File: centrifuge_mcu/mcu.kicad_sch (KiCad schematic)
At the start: 21 parts, among them J1 Conn_02x10_Odd_Even

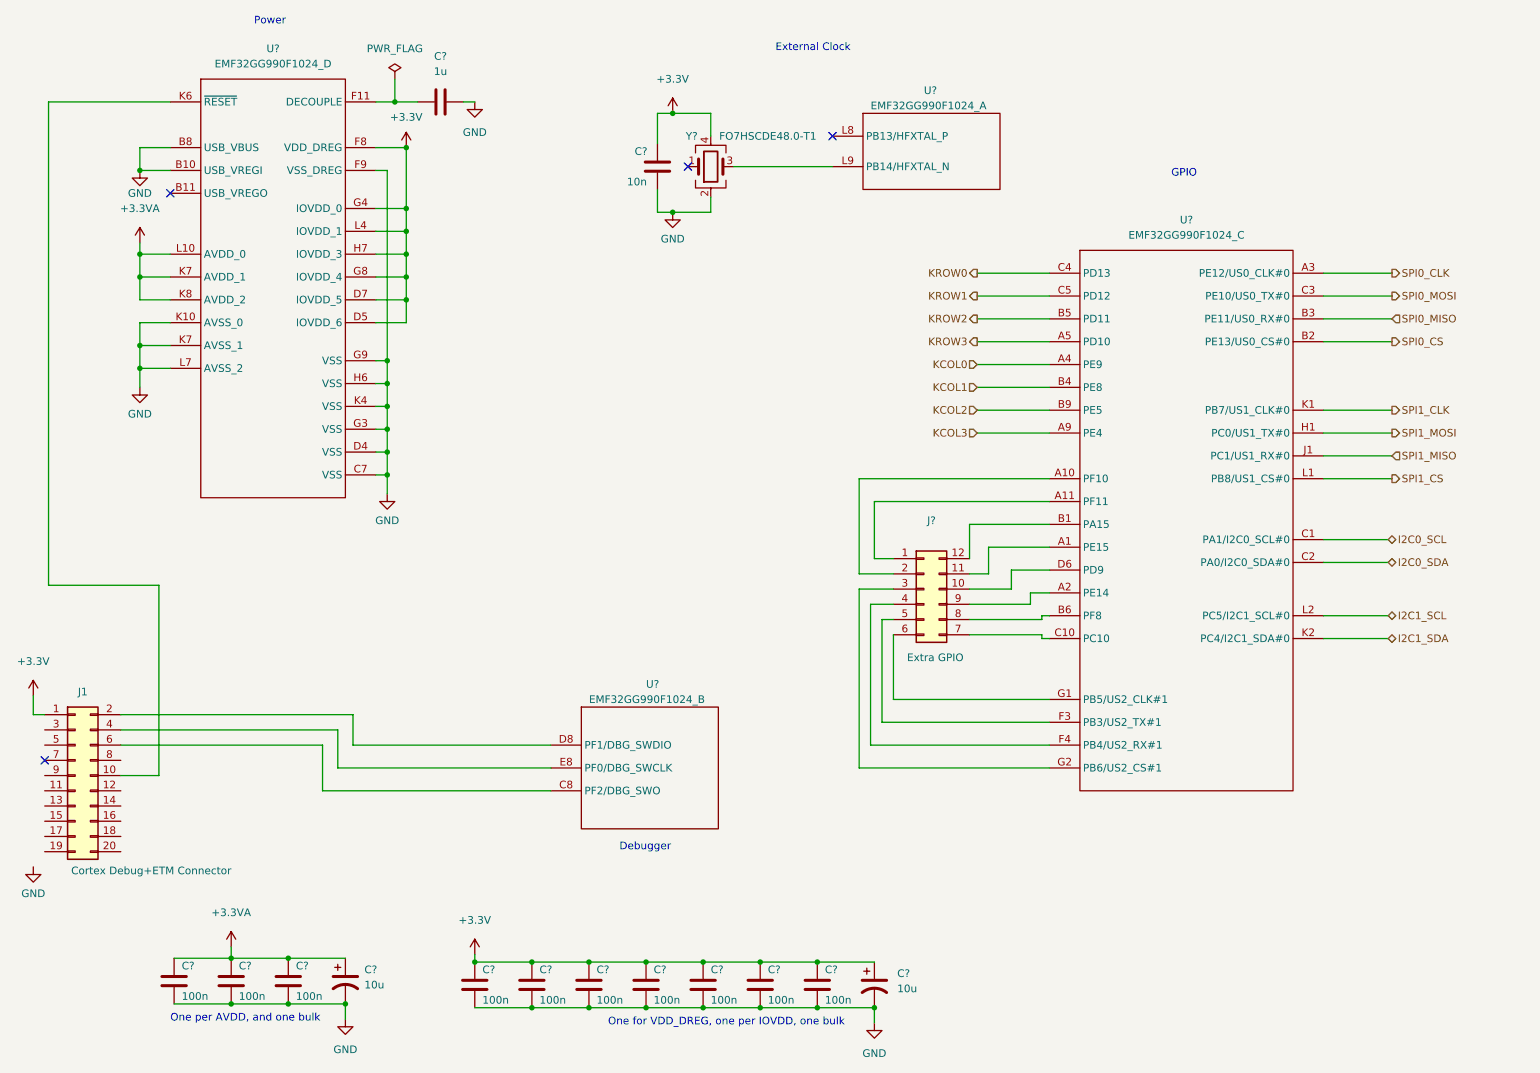
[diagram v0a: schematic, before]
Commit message: make and pick footprints for almost everything
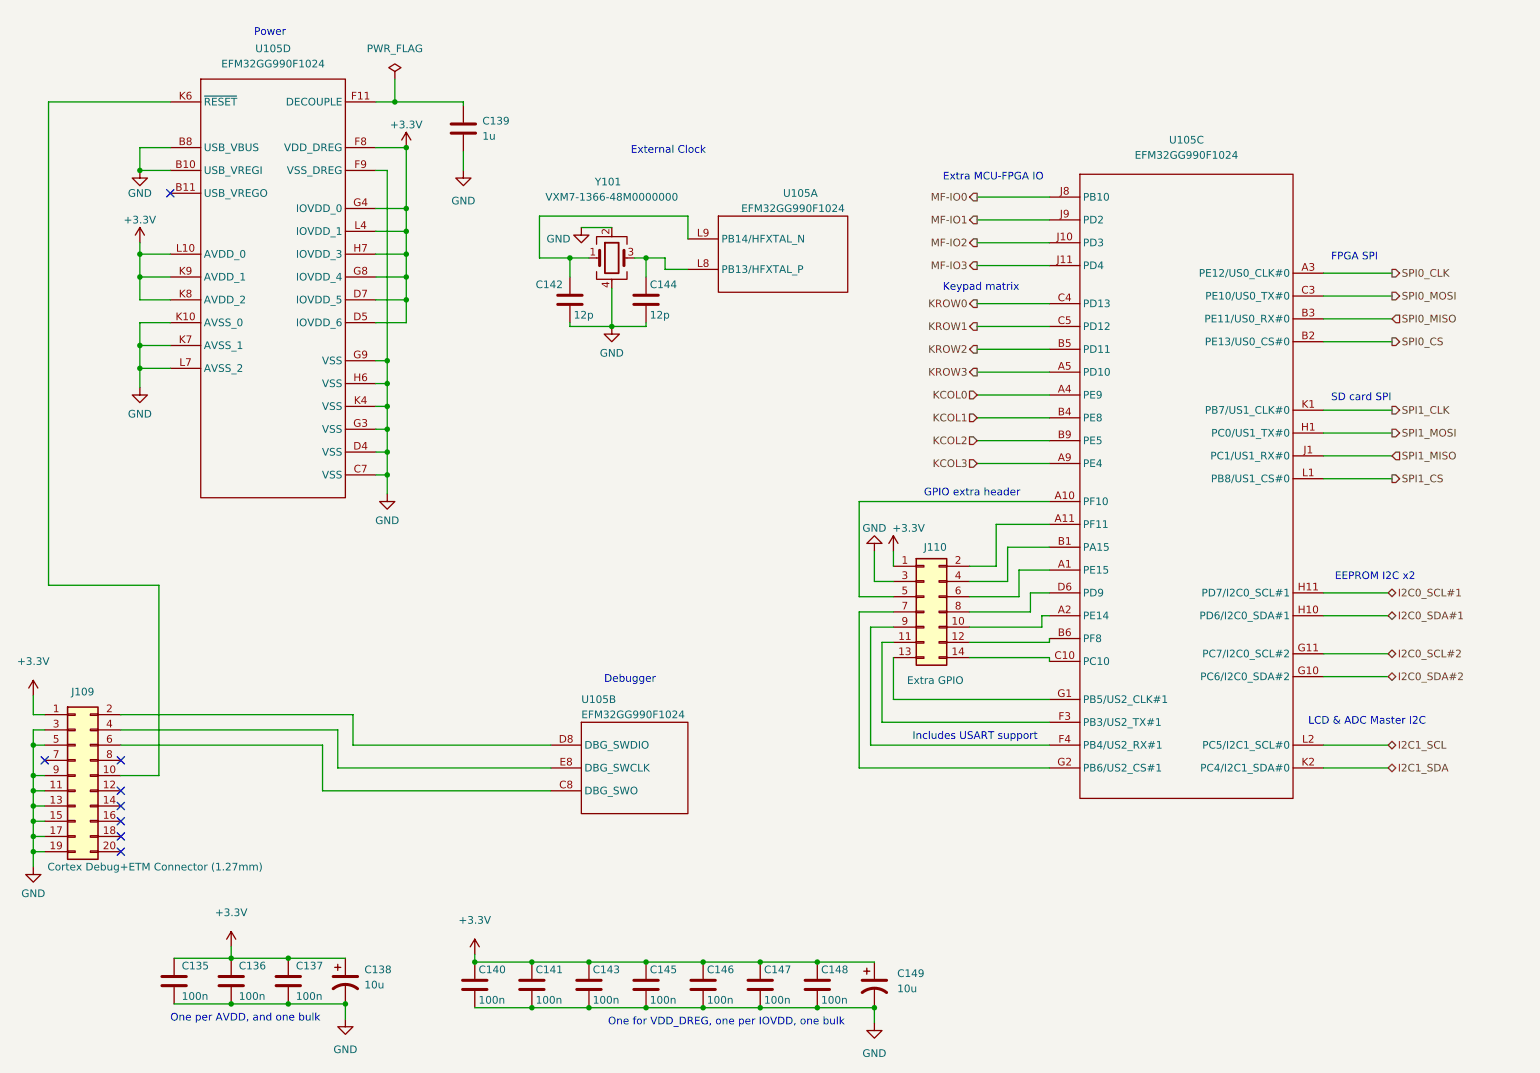
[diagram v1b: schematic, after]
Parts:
- removed C?: 10n, symbol Device:C
- removed U?: EMF32GG990F1024_B, symbol mcu_centrifuge_library:EMF32GG990F1024_B
- removed U?: EMF32GG990F1024_C, symbol mcu_centrifuge_library:EMF32GG990F1024_C
- removed U?: EMF32GG990F1024_D, symbol mcu_centrifuge_library:EMF32GG990F1024_D
- removed U?: EMF32GG990F1024_A, symbol mcu_centrifuge_library:EMF32GG990F1024_A
- removed Y?: FO7HSCDE48.0-T1, symbol Device:Crystal_GND24
- added C142, C144: 12p, Capacitor_SMD:C_0805_2012Metric_Pad1.18x1.45mm_HandSolder, symbol Device:C
- added U105: EFM32GG990F1024, symbol mcu_centrifuge_library:EFM32GG990F1024
- added Y101: VXM7-1366-48M0000000, Crystal:Crystal_SMD_TXC_7M-4Pin_3.2x2.5mm_HandSoldering, symbol Device:Crystal_GND24
- C135, C136, C137, C140, C141, C143, C145, C146, C147, C148: renamed from C?; footprint (none) -> Capacitor_SMD:C_0805_2012Metric_Pad1.18x1.45mm_HandSolder; Purchase (none) -> https://www.digikey.no/no/products/detail/taiyo-yuden/LMF21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
- C138, C149: renamed from C?; footprint (none) -> Capacitor_SMD:CP_Elec_4x5.4; Purchase (none) -> https://www.digikey.no/no/products/detail/nichicon/UWT1C100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
- C139: renamed from C?; footprint (none) -> Capacitor_SMD:C_0805_2012Metric_Pad1.18x1.45mm_HandSolder; Purchase (none) -> https://www.digikey.no/no/products/detail/kemet/C0805C105J4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
- J109: renamed from J1; footprint (none) -> Connector_PinHeader_1.27mm:PinHeader_2x10_P1.27mm_Vertical; Size Cortex Debug+ETM Connector -> Cortex Debug+ETM Connector (1.27mm)
- J110: renamed from J?; value Conn_02x06_Counter_Clockwise -> Conn_02x07_Counter_Clockwise; footprint (none) -> Connector_PinHeader_2.54mm:PinHeader_2x07_P2.54mm_Vertical; symbol Connector_Generic:Conn_02x06_Counter_Clockwise -> Connector_Generic:Conn_02x07_Odd_Even
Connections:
- net +3.3VA is gone; now on net +3.3V: C135.1, C136.1, C137.1, C138.1
- net +3.3V: now also J110.1 (Pin_1), U105.D5 (IOVDD_6), U105.D7 (IOVDD_5), U105.F8 (VDD_DREG), U105.G4 (IOVDD_0), U105.G8 (IOVDD_4), U105.H7 (IOVDD_3), U105.K8 (AVDD_2), U105.K9 (AVDD_1), U105.L10 (AVDD_0), U105.L4 (IOVDD_1)
- net GND: now also C139.1, J109.11 (Pin_11), J109.13 (Pin_13), J109.15 (Pin_15), J109.17 (Pin_17), J109.19 (Pin_19), J109.3 (Pin_3), J109.5 (Pin_5), J109.9 (Pin_9), J110.3 (Pin_3), C142.2, C144.2, U105.B10 (USB_VREGI), U105.B8 (USB_VBUS), U105.C7 (VSS), U105.D4 (VSS), U105.F9 (VSS_DREG), U105.G3 (VSS), U105.G9 (VSS), U105.H6 (VSS), U105.K10 (AVSS_0), U105.K4 (VSS), U105.K7 (AVSS_1), U105.L7 (AVSS_2), Y101.2, Y101.4; no longer C139.2
- net I2C1_SCL: now also U105.L2 (PC5/I2C1_SCL#0)
- net I2C1_SDA: now also U105.K2 (PC4/I2C1_SDA#0)
- net KCOL0: now also U105.A4 (PE9)
- net KCOL1: now also U105.B4 (PE8)
- net KCOL2: now also U105.B9 (PE5)
- net KCOL3: now also U105.A9 (PE4)
- net KROW0: now also U105.C4 (PD13)
- net KROW1: now also U105.C5 (PD12)
- net KROW2: now also U105.B5 (PD11)
- net KROW3: now also U105.A5 (PD10)
- net SPI0_CLK: now also U105.A3 (PE12/US0_CLK#0)
- net SPI0_CS: now also U105.B2 (PE13/US0_CS#0)
- net SPI0_MISO: now also U105.B3 (PE11/US0_RX#0)
- net SPI0_MOSI: now also U105.C3 (PE10/US0_TX#0)
- net SPI1_CLK: now also U105.K1 (PB7/US1_CLK#0)
- net SPI1_CS: now also U105.L1 (PB8/US1_CS#0)
- net SPI1_MISO: now also U105.J1 (PC1/US1_RX#0)
- net SPI1_MOSI: now also U105.H1 (PC0/US1_TX#0)
- net at J109.6 (Pin_6): now also U105.C8 (DBG_SWO)
- net at J109.2 (Pin_2): now also U105.D8 (DBG_SWDIO)
- net at J109.4 (Pin_4): now also U105.E8 (DBG_SWCLK)
- net at J109.10 (Pin_10): now also U105.K6 (~{RESET})
- net at J110.11 (Pin_11): now also U105.F3 (PB3/US2_TX#1)
- net at J110.2 (Pin_2): now also U105.A11 (PF11)
- net at J110.9 (Pin_9): now also U105.F4 (PB4/US2_RX#1)
- net at J110.12 (Pin_12): now also U105.B6 (PF8)
- net at J110.8 (Pin_8): now also U105.D6 (PD9)
- net at J110.7 (Pin_7): now also U105.G2 (PB6/US2_CS#1)
- net at J110.10 (Pin_10): now also U105.A2 (PE14)
- net at J110.5 (Pin_5): now also U105.A10 (PF10)
- net at J110.4 (Pin_4): now also U105.B1 (PA15)
- net at J110.6 (Pin_6): now also U105.A1 (PE15)
- new net: C142.1, U105.L9 (PB14/HFXTAL_N), Y101.1
- new net: C144.1, U105.L8 (PB13/HFXTAL_P), Y101.3
- new net: J110.13 (Pin_13), U105.G1 (PB5/US2_CLK#1)
- new net: J110.14 (Pin_14), U105.C10 (PC10)
- new net: C139.2, U105.F11 (DECOUPLE)
- new net I2C0_SCL#1: U105.H11 (PD7/I2C0_SCL#1)
- new net I2C0_SCL#2: U105.G11 (PC7/I2C0_SCL#2)
- new net I2C0_SDA#1: U105.H10 (PD6/I2C0_SDA#1)
- new net I2C0_SDA#2: U105.G10 (PC6/I2C0_SDA#2)
- new net MF-IO0: U105.J8 (PB10)
- new net MF-IO1: U105.J9 (PD2)
- new net MF-IO2: U105.J10 (PD3)
- new net MF-IO3: U105.J11 (PD4)
- no-connect marks 4 -> 8
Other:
- note added: "EEPROM I2C x2"
- note added: "Extra MCU-FPGA IO"
- note added: "FPGA SPI"
- note added: "GPIO extra header"
- note added: "Includes USART support"
- note added: "Keypad matrix"
- note added: "LCD & ADC Master I2C"
- note added: "SD card SPI"
- note removed: "GPIO"
- moved on the sheet: C139
